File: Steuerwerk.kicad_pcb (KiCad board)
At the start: 2 copper layers, 100 x 160 mm, 131 parts, among them J1 2PinTerminalBlocktg, J10 2PinTerminalBlocktg, J11 2PinTerminalBlocktg, J12 2PinTerminalBlocktg, J2 2PinTerminalBlocktg, J3 3PinTerminalBlocktg, J4 3PinTerminalBlocktg, J5 2PinTerminalBlocktg, J6 2PinTerminalBlocktg, J7 2PinTerminalBlocktg, J8 2PinTerminalBlocktg, J9 2PinTerminalBlocktg, Q1 Q_PNP_BCE, U1 74ls240, U2 74541, U3 74LS161, U4 74LS138, U5 74LS138, U6 74541, U7 74LS374, U8 74LS374

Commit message: Pin Anordnung von 374 korrigiert, manche Fehler gefunden und Todo Liste erweitert
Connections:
- D33 pad 2: VCC -> Net-(D33-Pad2)
- R25 pad 2: VCC -> Net-(D33-Pad2)
- R32 pad 2: /Takt -> Net-(D42-Pad2)
- U7 pad 12: /5 -> /7
- U7 pad 14: VCC -> Net-(D33-Pad2)
- U7 pad 15: Net-(J7-Pad2) -> /5
- U7 pad 16: /7 -> /3
- U7 pad 19: /enAkku -> /clrMPC
- U7 pad 2: /clrMPC -> Net-(U2-Pad8)
- U7 pad 5: Net-(U2-Pad8) -> Net-(J6-Pad2)
- U7 pad 6: /3 -> Net-(J7-Pad2)
- U7 pad 9: Net-(J6-Pad2) -> /enAkku
- U8 pad 12: /13 -> /15
- U8 pad 15: Net-(J11-Pad2) -> /13
- U8 pad 16: /15 -> /11
- U8 pad 17: Net-(D47-Pad2) -> Net-(D46-Pad2)
- U8 pad 18: /Takt -> Net-(D42-Pad2)
- U8 pad 19: /16 -> /9
- U8 pad 2: /9 -> Net-(J9-Pad2)
- U8 pad 4: Net-(D46-Pad2) -> Net-(D47-Pad2)
- U8 pad 5: Net-(J9-Pad2) -> Net-(J10-Pad2)
- U8 pad 6: /11 -> Net-(J11-Pad2)
- U8 pad 9: Net-(J10-Pad2) -> /16
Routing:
- net Net-(D42-Pad2): track 0.00 -> 46.6 mm
- net /Takt: track 46.6 -> 0.00 mm
- net VCC: track 770.9 -> 725.2 mm
- net Net-(D33-Pad2): track 0.00 -> 45.7 mm
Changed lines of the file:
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@@
-(kicad_pcb (version 20171130) (host pcbnew 5.0.0-rc2-unknown-81af2db~65~ubuntu16.04.1)
+(kicad_pcb (version 20171130) (host pcbnew 5.0.0-rc2-unknown-fc71fc6~65~ubuntu16.04.1)
   (general
     (thickness 1.6)
@@
     (zones 0)
     (modules 131)
-    (nets 136)
+    (nets 137)
   )
   (page A4)
@@
       (hpglpennumber 1)
       (hpglpenspeed 20)
-      (hpglpendiameter 15)
+      (hpglpendiameter 15.000000)
       (psnegative false)
       (psa4output false)
@@
   (net 134 "Net-(RP2-Pad2)")
   (net 135 "Net-(RP2-Pad1)")
+  (net 136 "Net-(D33-Pad2)")
   (net_class Default "This is the default net class."
     (clearance 0.2)
@@
     (add_net "Net-(D32-Pad1)")
     (add_net "Net-(D33-Pad1)")
+    (add_net "Net-(D33-Pad2)")
     (add_net "Net-(D34-Pad1)")
     (add_net "Net-(D35-Pad1)")
@@
     (fp_line (start 1.93 -1.25) (end 1.93 1.25) (layer F.Fab) (width 0.1))
     (pad 2 thru_hole oval (at 10.16 0 270) (size 1.6 1.6) (drill 0.8) (layers *.Cu *.Mask)
-      (net 65 VCC))
+      (net 136 "Net-(D33-Pad2)"))
     (pad 1 thru_hole circle (at 0 0 270) (size 1.6 1.6) (drill 0.8) (layers *.Cu *.Mask)
       (net 65 VCC))
@@
       (net 65 VCC))
     (pad 2 thru_hole oval (at 10.16 0 270) (size 1.6 1.6) (drill 0.8) (layers *.Cu *.Mask)
-      (net 42 /Takt))
+      (net 101 "Net-(D42-Pad2)"))
     (model ${KISYS3DMOD}/Resistors_THT.3dshapes/R_Axial_DIN0207_L6.3mm_D2.5mm_P10.16mm_Horizontal.wrl
       (at (xyz 0 0 0))
@@
       (net 42 /Takt))
     (pad 2 thru_hole oval (at 0 2.54 90) (size 2.4 1.6) (drill 0.8) (layers *.Cu *.Mask)
-      (net 66 /clrMPC))
+      (net 112 "Net-(U2-Pad8)"))
     (pad 12 thru_hole oval (at 7.62 20.32 90) (size 2.4 1.6) (drill 0.8) (layers *.Cu *.Mask)
-      (net 105 /5))
+      (net 106 /7))
     (pad 3 thru_hole oval (at 0 5.08 90) (size 2.4 1.6) (drill 0.8) (layers *.Cu *.Mask)
       (net 76 "Net-(D21-Pad2)"))
@@
       (net 78 "Net-(D30-Pad2)"))
     (pad 14 thru_hole oval (at 7.62 15.24 90) (size 2.4 1.6) (drill 0.8) (layers *.Cu *.Mask)
-      (net 65 VCC))
+      (net 136 "Net-(D33-Pad2)"))
     (pad 5 thru_hole oval (at 0 10.16 90) (size 2.4 1.6) (drill 0.8) (layers *.Cu *.Mask)
-      (net 112 "Net-(U2-Pad8)"))
+      (net 113 "Net-(J6-Pad2)"))
     (pad 15 thru_hole oval (at 7.62 12.7 90) (size 2.4 1.6) (drill 0.8) (layers *.Cu *.Mask)
-      (net 114 "Net-(J7-Pad2)"))
+      (net 105 /5))
     (pad 6 thru_hole oval (at 0 12.7 90) (size 2.4 1.6) (drill 0.8) (layers *.Cu *.Mask)
-      (net 104 /3))
+      (net 114 "Net-(J7-Pad2)"))
     (pad 16 thru_hole oval (at 7.62 10.16 90) (size 2.4 1.6) (drill 0.8) (layers *.Cu *.Mask)
-      (net 106 /7))
+      (net 104 /3))
     (pad 7 thru_hole oval (at 0 15.24 90) (size 2.4 1.6) (drill 0.8) (layers *.Cu *.Mask)
       (net 111 "Net-(R27-Pad2)"))
@@
       (net 75 "Net-(D17-Pad2)"))
     (pad 9 thru_hole oval (at 0 20.32 90) (size 2.4 1.6) (drill 0.8) (layers *.Cu *.Mask)
-      (net 113 "Net-(J6-Pad2)"))
-    (pad 19 thru_hole oval (at 7.62 2.54 90) (size 2.4 1.6) (drill 0.8) (layers *.Cu *.Mask)
       (net 67 /enAkku))
+    (pad 19 thru_hole oval (at 7.62 2.54 90) (size 2.4 1.6) (drill 0.8) (layers *.Cu *.Mask)
+      (net 66 /clrMPC))
     (pad 10 thru_hole oval (at 0 22.86 90) (size 2.4 1.6) (drill 0.8) (layers *.Cu *.Mask)
       (net 1 GND))
@@
       (net 79 "Net-(D33-Pad1)"))
     (pad 2 smd circle (at -2.199704 1.27 210) (size 1 1) (layers F.Cu F.Paste F.Mask)
-      (net 65 VCC))
+      (net 136 "Net-(D33-Pad2)"))
     (model ${KISYS3DMOD}/LEDs.3dshapes/LED_D1.8mm_W3.3mm_H2.4mm.wrl
       (at (xyz 0 0 0))
@@
       (net 1 GND))
     (pad 19 thru_hole oval (at 7.62 2.54 90) (size 2.4 1.6) (drill 0.8) (layers *.Cu *.Mask)
-      (net 68 /16))
+      (net 107 /9))
     (pad 9 thru_hole oval (at 0 20.32 90) (size 2.4 1.6) (drill 0.8) (layers *.Cu *.Mask)
-      (net 116 "Net-(J10-Pad2)"))
+      (net 68 /16))
     (pad 18 thru_hole oval (at 7.62 5.08 90) (size 2.4 1.6) (drill 0.8) (layers *.Cu *.Mask)
-      (net 42 /Takt))
+      (net 101 "Net-(D42-Pad2)"))
     (pad 8 thru_hole oval (at 0 17.78 90) (size 2.4 1.6) (drill 0.8) (layers *.Cu *.Mask)
       (net 63 "Net-(R39-Pad2)"))
     (pad 17 thru_hole oval (at 7.62 7.62 90) (size 2.4 1.6) (drill 0.8) (layers *.Cu *.Mask)
-      (net 37 "Net-(D47-Pad2)"))
+      (net 35 "Net-(D46-Pad2)"))
     (pad 7 thru_hole oval (at 0 15.24 90) (size 2.4 1.6) (drill 0.8) (layers *.Cu *.Mask)
       (net 41 "Net-(D61-Pad2)"))
     (pad 16 thru_hole oval (at 7.62 10.16 90) (size 2.4 1.6) (drill 0.8) (layers *.Cu *.Mask)
-      (net 109 /15))
-    (pad 6 thru_hole oval (at 0 12.7 90) (size 2.4 1.6) (drill 0.8) (layers *.Cu *.Mask)
       (net 103 /11))
-    (pad 15 thru_hole oval (at 7.62 12.7 90) (size 2.4 1.6) (drill 0.8) (layers *.Cu *.Mask)
+    (pad 6 thru_hole oval (at 0 12.7 90) (size 2.4 1.6) (drill 0.8) (layers *.Cu *.Mask)
       (net 117 "Net-(J11-Pad2)"))
+    (pad 15 thru_hole oval (at 7.62 12.7 90) (size 2.4 1.6) (drill 0.8) (layers *.Cu *.Mask)
+      (net 108 /13))
     (pad 5 thru_hole oval (at 0 10.16 90) (size 2.4 1.6) (drill 0.8) (layers *.Cu *.Mask)
-      (net 115 "Net-(J9-Pad2)"))
+      (net 116 "Net-(J10-Pad2)"))
     (pad 14 thru_hole oval (at 7.62 15.24 90) (size 2.4 1.6) (drill 0.8) (layers *.Cu *.Mask)
       (net 40 "Net-(D59-Pad2)"))
     (pad 4 thru_hole oval (at 0 7.62 90) (size 2.4 1.6) (drill 0.8) (layers *.Cu *.Mask)
-      (net 35 "Net-(D46-Pad2)"))
+      (net 37 "Net-(D47-Pad2)"))
     (pad 13 thru_hole oval (at 7.62 17.78 90) (size 2.4 1.6) (drill 0.8) (layers *.Cu *.Mask)
       (net 62 "Net-(R38-Pad2)"))
@@
       (net 34 "Net-(D43-Pad2)"))
     (pad 12 thru_hole oval (at 7.62 20.32 90) (size 2.4 1.6) (drill 0.8) (layers *.Cu *.Mask)
-      (net 108 /13))
+      (net 109 /15))
     (pad 2 thru_hole oval (at 0 2.54 90) (size 2.4 1.6) (drill 0.8) (layers *.Cu *.Mask)
-      (net 107 /9))
+      (net 115 "Net-(J9-Pad2)"))
     (pad 11 thru_hole oval (at 7.62 22.86 90) (size 2.4 1.6) (drill 0.8) (layers *.Cu *.Mask)
       (net 42 /Takt))
@@
   (segment (start 125.73 70.87) (end 125.73 117.399998) (width 1.25) (layer B.Cu) (net 41) (status 400000))
   (segment (start 125.73 117.399998) (end 125.766 117.435998) (width 1.25) (layer B.Cu) (net 41))
-  (segment (start 106.68 70.87) (end 106.68 117.399998) (width 1.25) (layer B.Cu) (net 42) (status 400000))
-  (segment (start 106.68 117.399998) (end 106.716 117.435998) (width 1.25) (layer B.Cu) (net 42))
+  (segment (start 106.68 70.87) (end 106.68 117.399998) (width 1.25) (layer B.Cu) (net 101) (status 400000))
+  (segment (start 106.68 117.399998) (end 106.716 117.435998) (width 1.25) (layer B.Cu) (net 101))
   (segment (start 54.95 176.93) (end 54.95 176.921998) (width 1.25) (layer B.Cu) (net 45) (status C00000))
   (segment (start 54.95 176.921998) (end 56.806 175.065998) (width 1.25) (layer B.Cu) (net 45) (status 400000))
@@
   (segment (start 133.35 70.87) (end 133.35 118.034998) (width 1.25) (layer B.Cu) (net 63) (status 400000))
   (segment (start 133.35 118.034998) (end 133.386 118.070998) (width 1.25) (layer B.Cu) (net 63))
-  (segment (start 85.09 71.12) (end 85.09 116.764998) (width 1.25) (layer B.Cu) (net 65) (status 400000))
-  (segment (start 85.09 116.764998) (end 85.126 116.800998) (width 1.25) (layer B.Cu) (net 65))
+  (segment (start 85.09 71.12) (end 85.09 116.764998) (width 1.25) (layer B.Cu) (net 136) (status 400000))
+  (segment (start 85.09 116.764998) (end 85.126 116.800998) (width 1.25) (layer B.Cu) (net 136))
   (segment (start 66.04 96.52) (end 135.251998 96.52) (width 1.25) (layer F.Cu) (net 65) (status 400000))
   (segment (start 135.251998 96.52) (end 135.291 96.480998) (width 1.25) (layer F.Cu) (net 65))

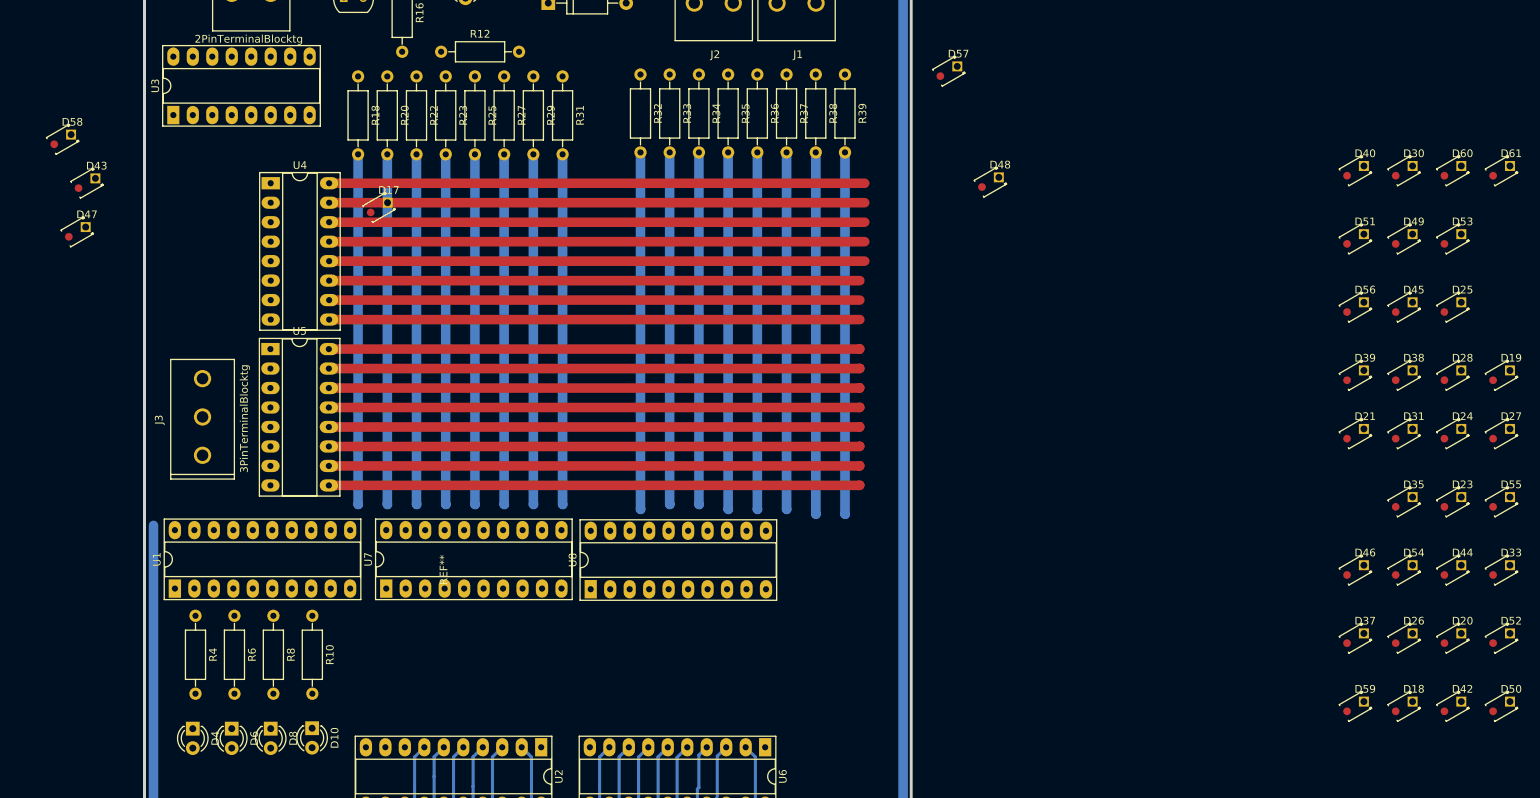
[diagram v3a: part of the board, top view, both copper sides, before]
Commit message: kleine LEDs auf ihren Platz gelegt
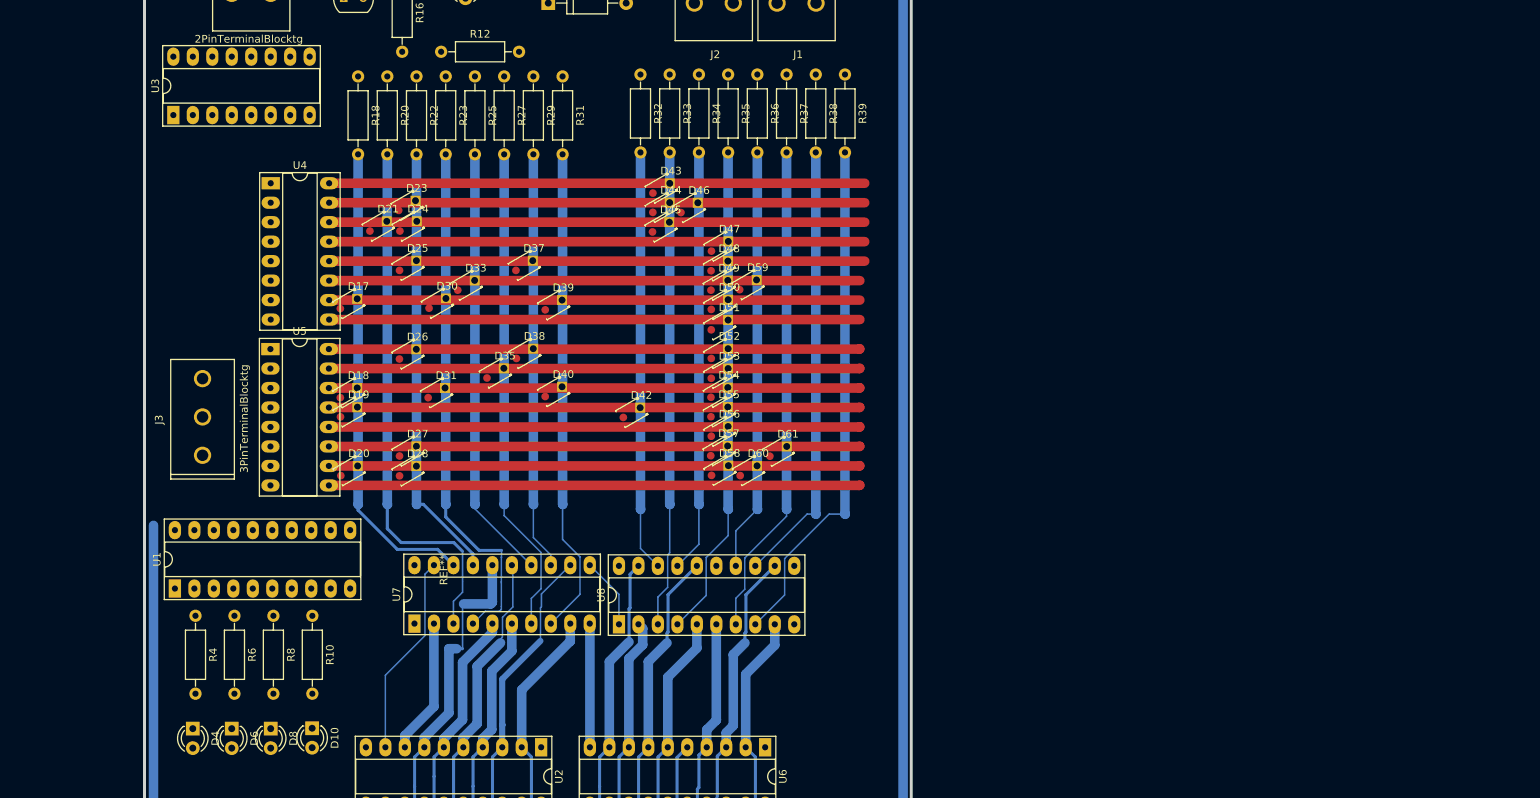
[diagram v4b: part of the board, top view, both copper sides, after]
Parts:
- moved D19 150.4 mm to (69.8, 104.1)
- moved D20 145.6 mm to (69.8, 111.8)
- moved D18 143.6 mm to (69.7, 101.6)
- moved D27 142.6 mm to (77.5, 109.2)
- moved D23 141.8 mm to (77.3, 77.2)
- moved D33 140.0 mm to (85.0, 87.6)
- moved D24 138.9 mm to (77.5, 79.9)
- moved D28 136.8 mm to (77.5, 111.8)
- moved D25 136.4 mm to (77.5, 85.0)
- moved D26 135.1 mm to (77.4, 96.5)
- moved D21 130.3 mm to (73.6, 79.9)
- moved D30 127.2 mm to (81.3, 89.9)
- moved D31 126.3 mm to (81.2, 101.6)
- moved D35 119.7 mm to (88.9, 99.0)
- moved D37 118.8 mm to (92.6, 85.0)
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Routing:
- net /3: track 57.9 -> 88.4 mm
- net /7: track 53.3 -> 80.8 mm
- net /5: track 55.5 -> 82.0 mm
- net /clrMPC: track 0.00 -> 26.4 mm
- net /11: track 53.8 -> 80.0 mm
- net /15: track 58.1 -> 84.4 mm
- net /9: track 55.0 -> 80.2 mm
- net Net-(D21-Pad2): track 45.7 -> 69.8 mm
- net Net-(D30-Pad2): track 45.7 -> 68.6 mm
- net Net-(R39-Pad2): track 47.2 -> 67.6 mm
- net Net-(J6-Pad2): track 56.5 -> 75.3 mm
- net /enAkku: track 53.3 -> 72.1 mm
- net Net-(D39-Pad2): track 45.7 -> 63.8 mm
- net Net-(R27-Pad2): track 45.7 -> 63.8 mm
- net Net-(D61-Pad2): track 46.6 -> 64.3 mm
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
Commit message: Teile geordnet und Notiz hinzugefügt
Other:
- board text added: "<- 1OK Resistoren"
- board text added: "Kondensatoren"

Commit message: Überflüssige LEDs entfernt, 1k Resistoren Eingebaut, Teile geordnet
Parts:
- removed R18, R20, R22, R23, R25, R27, R29, R31, R32, R33, R34, R35, R36, R37, R38, R39: R, Resistors_ThroughHole:R_Axial_DIN0207_L6.3mm_D2.5mm_P10.16mm_Horizontal
- removed REF**: EuroBoard160mmX100mm_holes, EuroBoard_Outline:EuroBoard160mmX100mm_holes
- moved C5 152.5 mm to (96.9, 154.8), turned to 90 degrees
- moved C6 147.2 mm to (67.6, 140.9), turned to 90 degrees
- moved R16 135.1 mm to (-59.5, 48.2)
- moved C3 131.8 mm to (59.9, 117.3)
- moved C4 118.3 mm to (99.7, 130.6), turned to 90 degrees
- moved RP1 116.0 mm to (82.5, 68.2)
- moved C1 106.0 mm to (59.9, 93.3)
- moved D42 100.6 mm to (207.2, 105.4)
- moved D18 100.6 mm to (170.3, 102.9)
- moved D20 100.6 mm to (170.4, 113.0)
- moved D26 100.6 mm to (178.0, 97.8)
- moved D31 100.6 mm to (181.8, 102.9)
- moved D35 100.6 mm to (189.4, 100.3)
- moved D38 100.6 mm to (193.3, 97.7)
- moved D52 100.6 mm to (218.7, 97.7)
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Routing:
- net Net-(D21-Pad2): track 69.8 -> 0.00 mm
- net Net-(D30-Pad2): track 68.6 -> 0.00 mm
- net Net-(U8-Pad8): track 67.6 -> 0.00 mm
- net Net-(D61-Pad2): track 64.3 -> 0.00 mm
- net Net-(D47-Pad2): track 64.3 -> 0.00 mm
- net Net-(D39-Pad2): track 63.8 -> 0.00 mm
- net Net-(U7-Pad7): track 63.8 -> 0.00 mm
- net Net-(D43-Pad2): track 62.2 -> 0.00 mm
- net Net-(D17-Pad2): track 61.9 -> 0.00 mm
- net Net-(U8-Pad13): track 57.9 -> 0.00 mm
- net Net-(D23-Pad2): track 57.2 -> 0.00 mm
- net Net-(D33-Pad2): track 56.7 -> 0.00 mm
- net Net-(D59-Pad2): track 55.1 -> 0.00 mm
- net Net-(D46-Pad2): track 55.1 -> 0.00 mm
- net Net-(D42-Pad2): track 54.9 -> 0.00 mm
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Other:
- board outline removed
- board text removed: "<- 1OK Resistoren"
- board text removed: "Kondensatoren"
